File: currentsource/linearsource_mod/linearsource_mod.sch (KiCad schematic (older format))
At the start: 18 parts, among them P1 CONN_01X04, P2 CONN_01X04, Q1 PSMN017-30BL, Q2 BC849, U1 LM358

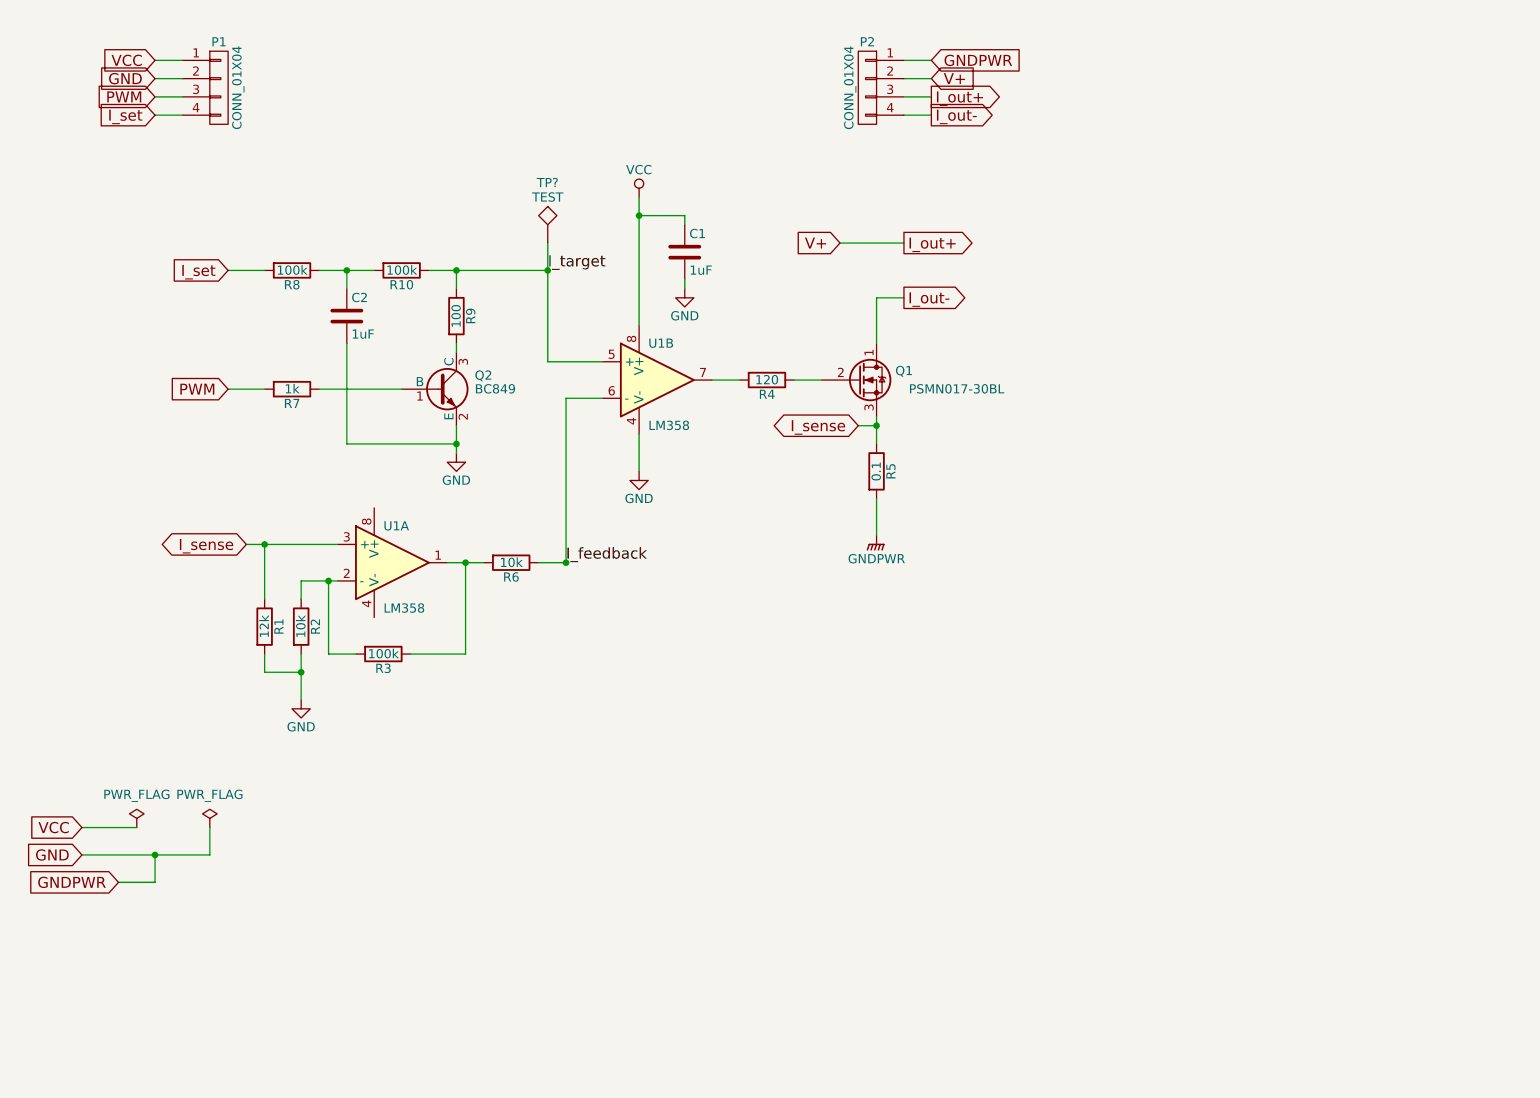
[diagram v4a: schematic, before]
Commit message: currentousrce: Change to edge header, incl Ifeedback
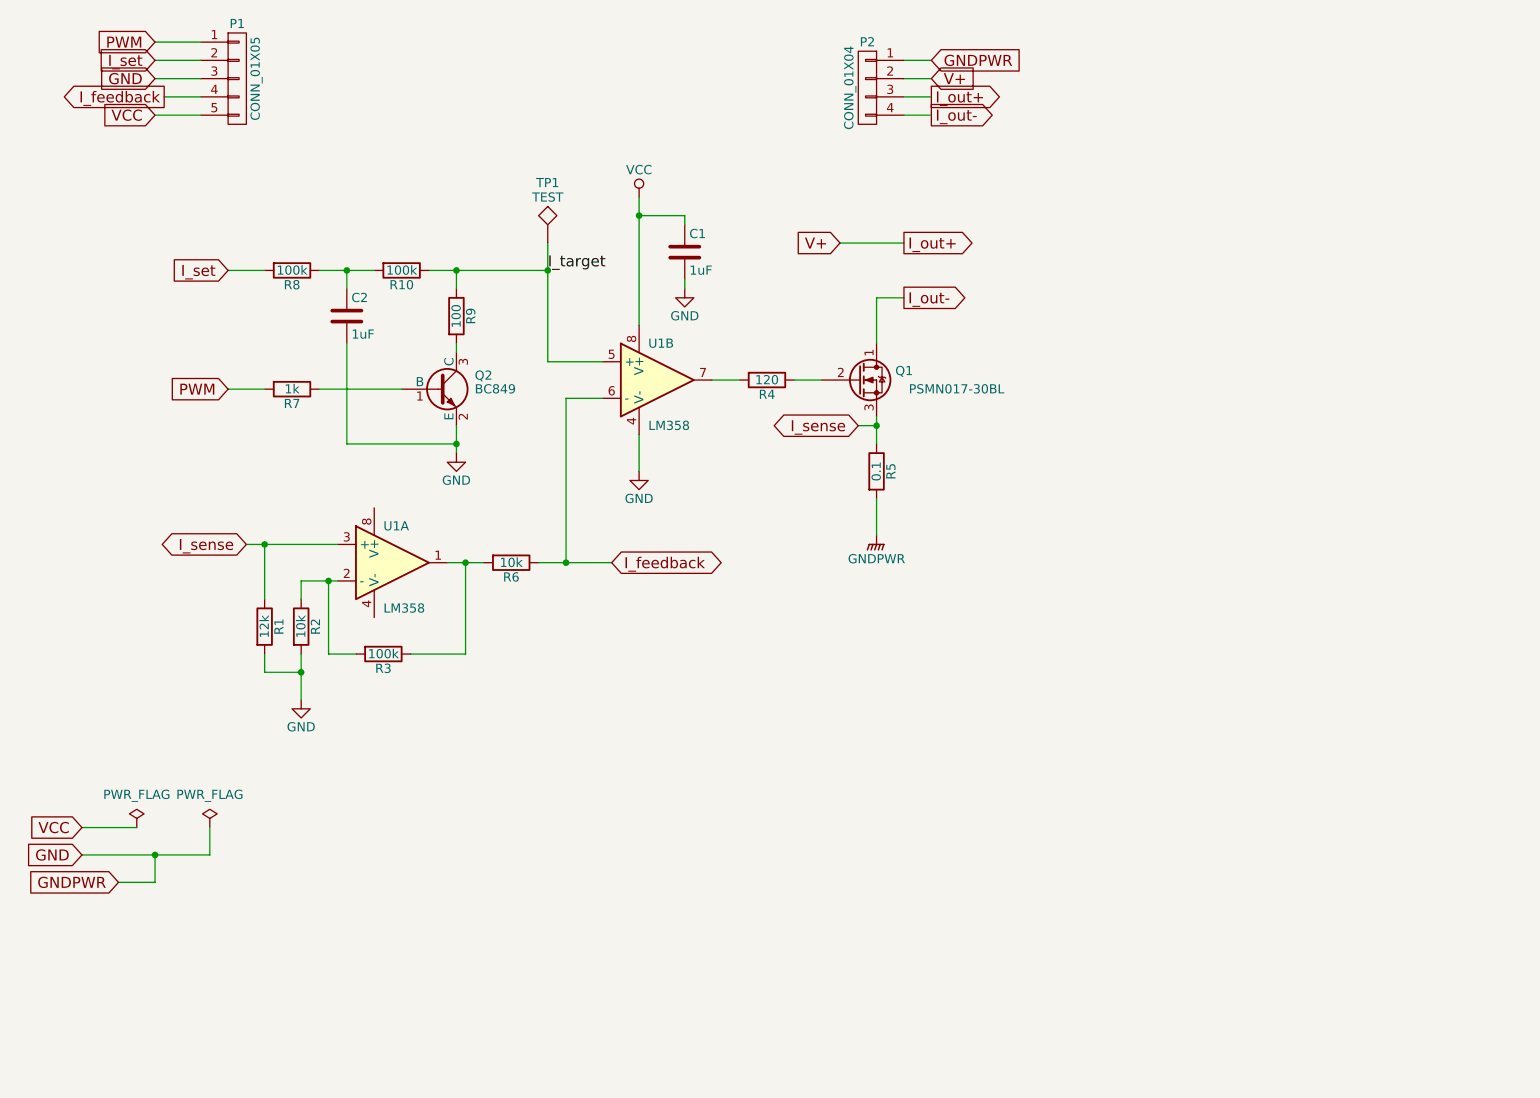
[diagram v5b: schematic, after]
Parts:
- removed P1: CONN_01X04, Pin_Headers:Pin_Header_Straight_1x04, symbol CONN_01X04
- added P1: CONN_01X05, Edge:Pin_Header_Edge_1x05_Pitch2.54mm, symbol CONN_01X05
- TP1: renamed from TP?; footprint (none) -> SMD_Packages:1Pin
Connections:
- net GND: now also P1.3 (P3)
- net I_feedback: now also P1.4 (P4)
- net I_set: now also P1.2 (P2)
- net PWM: now also P1.1 (P1)
- net VCC: now also P1.5 (P5)
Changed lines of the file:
@@
 	2900 4100 2900 3600
 Wire Wire Line
-	2000 3700 2150 3700
-Wire Wire Line
-	2150 3700 2200 3700
+	2000 3700 2200 3700
 Wire Wire Line
 	2000 3700 2000 3800
@@
 $EndComp
 Wire Wire Line
-	3850 1600 3850 1700
-Wire Wire Line
-	3850 1700 3850 2300
+	3850 1600 3850 2300
 Wire Wire Line
 	4700 2600 4850 2600
 Wire Wire Line
-	5150 2800 5150 2850
-Wire Wire Line
-	5150 2850 5150 2950
+	5150 2800 5150 2950
 Wire Wire Line
 	5150 3250 5150 3450
 Connection ~ 5150 2850
 Wire Wire Line
-	2000 4100 2000 4200
-Wire Wire Line
-	2000 4200 2000 4350
+	2000 4100 2000 4350
 Wire Wire Line
 	1800 3800 1800 3500
 Wire Wire Line
-	1700 3500 1800 3500
-Wire Wire Line
-	1800 3500 2200 3500
+	1700 3500 2200 3500
 Wire Wire Line
 	1800 4100 1800 4200
@@
 	4250 2600 4400 2600
 Wire Wire Line
-	2800 3600 2900 3600
-Wire Wire Line
-	2900 3600 3000 3600
+	2800 3600 3000 3600
 $Comp
 L R R6
@@
 	1    0    0    -1
 $EndComp
-$Comp
-L CONN_01X04 P1
-U 1 1 57115F44
-P 1550 1000
-F 0 "P1" H 1550 1250 50  0000 C CNN
-F 1 "CONN_01X04" V 1650 1000 50  0000 C CNN
-F 2 "Pin_Headers:Pin_Header_Straight_1x04" H 1550 1000 50  0001 C CNN
-F 3 "" H 1550 1000 50  0000 C CNN
-	1    1550 1000
-	1    0    0    -1
-$EndComp
-Text GLabel 1200 850  0    60   Input ~ 0
+Text GLabel 1200 1150 0    60   Input ~ 0
 VCC
-Text GLabel 1200 1050 0    60   Input ~ 0
+Text GLabel 1200 750  0    60   Input ~ 0
 PWM
 Text GLabel 1200 950  0    60   Input ~ 0
 GND
-Text GLabel 1200 1150 0    60   Input ~ 0
+Text GLabel 1200 850  0    60   Input ~ 0
 I_set
 $Comp
@@
 Wire Wire Line
 	5450 850  5300 850
-Wire Wire Line
-	1200 850  1350 850
-Wire Wire Line
-	1200 1150 1350 1150
 $Comp
 L C C1
@@
 $EndComp
 Wire Wire Line
-	2850 2850 2850 2950
-Wire Wire Line
-	2850 2950 2850 3000
+	2850 2850 2850 3000
 Wire Wire Line
 	2850 2450 2850 2400
@@
 	3350 2500 3650 2500
 Wire Wire Line
-	2100 2000 2250 2000
-Wire Wire Line
-	2250 2000 2400 2000
-Wire Wire Line
-	2700 2000 2850 2000
-Wire Wire Line
-	2850 2000 3350 2000
-Wire Wire Line
-	3350 1850 3350 2000
-Wire Wire Line
-	3350 2000 3350 2500
+	2100 2000 2400 2000
+Wire Wire Line
+	2700 2000 3350 2000
+Wire Wire Line
+	3350 1850 3350 2500
 Wire Wire Line
 	2850 2000 2850 2100
@@
 	1600 2650 1800 2650
 Wire Wire Line
-	3450 3600 3300 3600
+	3300 3600 3700 3600
 Text Label 3350 2000 0    60   ~ 0
 I_target
-Text Label 3450 3600 0    60   ~ 0
-I_feedback
 Connection ~ 3450 3600
 Connection ~ 3350 2000
@@
 	1500 5200 1500 5050
 Wire Wire Line
-	800  5200 1200 5200
-Wire Wire Line
-	1200 5200 1500 5200
+	800  5200 1500 5200
 Wire Wire Line
 	1000 5350 1200 5350
@@
 	0    1    1    0
 $EndComp
-Wire Wire Line
-	1200 1050 1350 1050
-Wire Wire Line
-	1200 950  1350 950
-$Comp
-L TEST TP?
+$Comp
+L TEST TP1
 U 1 1 598733DB
 P 3350 1850
-F 0 "TP?" H 3350 2150 50  0000 C BNN
+F 0 "TP1" H 3350 2150 50  0000 C BNN
 F 1 "TEST" H 3350 2100 50  0000 C CNN
-F 2 "" H 3350 1850 50  0001 C CNN
+F 2 "SMD_Packages:1Pin" H 3350 1850 50  0001 C CNN
 F 3 "" H 3350 1850 50  0001 C CNN
 	1    3350 1850
 	1    0    0    -1
 $EndComp
+Text GLabel 3700 3600 2    60   BiDi ~ 0
+I_feedback
+$Comp
+L CONN_01X05 P1
+U 1 1 59873CDC
+P 1650 950
+F 0 "P1" H 1650 1250 50  0000 C CNN
+F 1 "CONN_01X05" V 1750 950 50  0000 C CNN
+F 2 "Edge:Pin_Header_Edge_1x05_Pitch2.54mm" H 1650 950 50  0001 C CNN
+F 3 "" H 1650 950 50  0001 C CNN
+	1    1650 950
+	1    0    0    -1
+$EndComp
+Text GLabel 1250 1050 0    60   Output ~ 0
+I_feedback
+Wire Wire Line
+	1200 950  1450 950
+Wire Wire Line
+	1250 1050 1450 1050
+Wire Wire Line
+	1200 1150 1450 1150
+Wire Wire Line
+	1200 850  1450 850
+Wire Wire Line
+	1200 750  1450 750
 $EndSCHEMATC

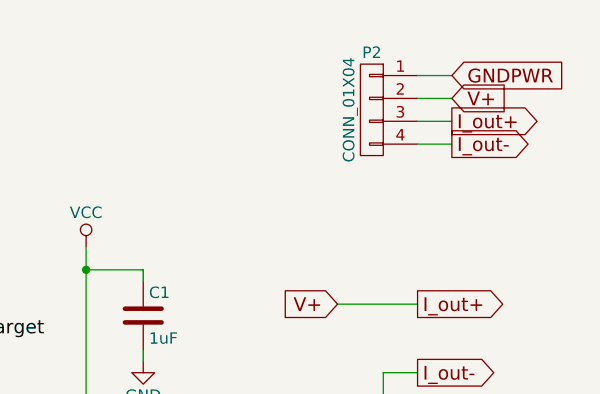
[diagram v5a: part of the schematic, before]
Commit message: currentsource: Use edge header also for power
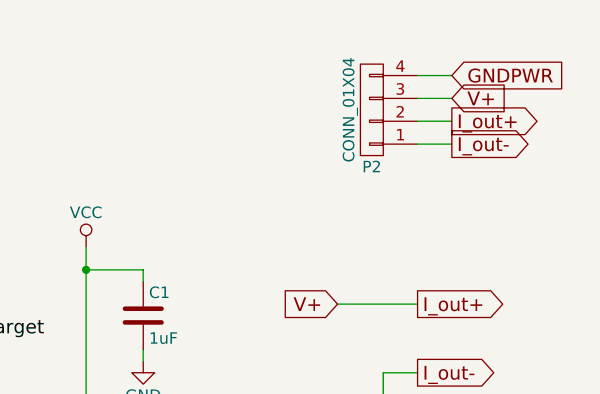
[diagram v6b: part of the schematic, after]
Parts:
- P2: footprint Pin_Headers:Pin_Header_Straight_1x04 -> (none)
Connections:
- net GND: now also P2.4 (P4); no longer P2.1 (P1)
- net I_out-: now also P2.1 (P1); no longer P2.4 (P4)
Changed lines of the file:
@@
 	1    0    0    -1
 $EndComp
-Wire Wire Line
-	2600 4100 2900 4100
-Wire Wire Line
-	2900 4100 2900 3600
-Wire Wire Line
-	2000 3700 2200 3700
-Wire Wire Line
-	2000 3700 2000 3800
-Wire Wire Line
-	2300 4100 2150 4100
-Wire Wire Line
-	2150 4100 2150 3700
-Connection ~ 2150 3700
-Wire Wire Line
-	3850 2900 3850 3100
 $Comp
 L VCC #PWR01
@@
 	1    0    0    -1
 $EndComp
-Wire Wire Line
-	3850 1600 3850 2300
-Wire Wire Line
-	4700 2600 4850 2600
-Wire Wire Line
-	5150 2800 5150 2950
-Wire Wire Line
-	5150 3250 5150 3450
-Connection ~ 5150 2850
-Wire Wire Line
-	2000 4100 2000 4350
-Wire Wire Line
-	1800 3800 1800 3500
-Wire Wire Line
-	1700 3500 2200 3500
-Wire Wire Line
-	1800 4100 1800 4200
-Wire Wire Line
-	1800 4200 2000 4200
-Connection ~ 2000 4200
 Text GLabel 5050 2850 0    60   BiDi ~ 0
 I_sense
-Wire Wire Line
-	5050 2850 5150 2850
 Text GLabel 1700 3500 0    60   BiDi ~ 0
 I_sense
-Connection ~ 1800 3500
-Connection ~ 2900 3600
-Wire Wire Line
-	5150 2150 5150 2400
-Wire Wire Line
-	4250 2600 4400 2600
-Wire Wire Line
-	2800 3600 3000 3600
 $Comp
 L R R6
@@
 	0    1    1    0
 $EndComp
-Wire Wire Line
-	3450 2700 3450 3600
-Wire Wire Line
-	3450 2700 3650 2700
 $Comp
 L GNDPWR #PWR02
@@
 Text GLabel 1200 850  0    60   Input ~ 0
 I_set
-$Comp
-L CONN_01X04 P2
-U 1 1 571160BF
-P 5100 1000
-F 0 "P2" H 5100 1250 50  0000 C CNN
-F 1 "CONN_01X04" V 5200 1000 50  0000 C CNN
-F 2 "Pin_Headers:Pin_Header_Straight_1x04" H 5100 1000 50  0001 C CNN
-F 3 "" H 5100 1000 50  0000 C CNN
-	1    5100 1000
-	-1   0    0    -1
-$EndComp
 Text GLabel 5450 850  2    60   Input ~ 0
 GNDPWR
@@
 Text GLabel 4950 1850 0    60   Input ~ 0
 V+
-Wire Wire Line
-	5450 1150 5300 1150
-Wire Wire Line
-	5450 1050 5300 1050
-Wire Wire Line
-	5450 950  5300 950
-Wire Wire Line
-	5450 850  5300 850
 $Comp
 L C C1
@@
 	1    0    0    -1
 $EndComp
-Wire Wire Line
-	4100 1700 4100 1750
-Wire Wire Line
-	4100 2050 4100 2100
 $Comp
 L GND #PWR03
@@
 	0    1    1    0
 $EndComp
-Wire Wire Line
-	2850 2850 2850 3000
-Wire Wire Line
-	2850 2450 2850 2400
-Wire Wire Line
-	2100 2650 2550 2650
-Wire Wire Line
-	3350 2500 3650 2500
-Wire Wire Line
-	2100 2000 2400 2000
-Wire Wire Line
-	2700 2000 3350 2000
-Wire Wire Line
-	3350 1850 3350 2500
-Wire Wire Line
-	2850 2000 2850 2100
 $Comp
 L C C2
@@
 	0    1    1    0
 $EndComp
-Wire Wire Line
-	2250 2000 2250 2100
-Connection ~ 2250 2000
-Connection ~ 2850 2000
 Text GLabel 1600 2000 0    60   Input ~ 0
 I_set
-Wire Wire Line
-	1600 2000 1800 2000
-Wire Wire Line
-	2250 2400 2250 2950
-Wire Wire Line
-	2250 2950 2850 2950
-Connection ~ 2850 2950
 Text GLabel 1600 2650 0    60   Input ~ 0
 PWM
-Wire Wire Line
-	1600 2650 1800 2650
-Wire Wire Line
-	3300 3600 3700 3600
 Text Label 3350 2000 0    60   ~ 0
 I_target
-Connection ~ 3450 3600
-Connection ~ 3350 2000
-Wire Wire Line
-	5300 2150 5150 2150
-Wire Wire Line
-	4950 1850 5300 1850
-Wire Wire Line
-	4100 1700 3850 1700
-Connection ~ 3850 1700
 Text GLabel 800  5050 0    60   Input ~ 0
 VCC
@@
 	1    0    0    -1
 $EndComp
-Wire Wire Line
-	1100 5050 800  5050
-Wire Wire Line
-	1500 5200 1500 5050
-Wire Wire Line
-	800  5200 1500 5200
-Wire Wire Line
-	1000 5350 1200 5350
-Wire Wire Line
-	1200 5350 1200 5200
-Connection ~ 1200 5200
 $Comp
 L R R10
@@
 I_feedback
 Wire Wire Line
+	2600 4100 2900 4100
+Wire Wire Line
+	2900 4100 2900 3600
+Wire Wire Line
+	2000 3700 2200 3700
+Wire Wire Line
+	2000 3700 2000 3800
+Wire Wire Line
+	2300 4100 2150 4100
+Wire Wire Line
+	2150 4100 2150 3700
+Connection ~ 2150 3700
+Wire Wire Line
+	3850 2900 3850 3100
+Wire Wire Line
+	3850 1600 3850 2300
+Wire Wire Line
+	4700 2600 4850 2600
+Wire Wire Line
+	5150 2800 5150 2950
+Wire Wire Line
+	5150 3250 5150 3450
+Connection ~ 5150 2850
+Wire Wire Line
+	2000 4100 2000 4350
+Wire Wire Line
+	1800 3800 1800 3500
+Wire Wire Line
+	1700 3500 2200 3500
+Wire Wire Line
+	1800 4100 1800 4200
+Wire Wire Line
+	1800 4200 2000 4200
+Connection ~ 2000 4200
+Wire Wire Line
+	5050 2850 5150 2850
+Connection ~ 1800 3500
+Connection ~ 2900 3600
+Wire Wire Line
+	5150 2150 5150 2400
+Wire Wire Line
+	4250 2600 4400 2600
+Wire Wire Line
+	2800 3600 3000 3600
+Wire Wire Line
+	3450 2700 3450 3600
+Wire Wire Line
+	3450 2700 3650 2700
+Wire Wire Line
+	4100 1700 4100 1750
+Wire Wire Line
+	4100 2050 4100 2100
+Wire Wire Line
+	2850 2850 2850 3000
+Wire Wire Line
+	2850 2450 2850 2400
+Wire Wire Line
+	2100 2650 2550 2650
+Wire Wire Line
+	3350 2500 3650 2500
+Wire Wire Line
+	2100 2000 2400 2000
+Wire Wire Line
+	2700 2000 3350 2000
+Wire Wire Line
+	3350 1850 3350 2500
+Wire Wire Line
+	2850 2000 2850 2100
+Wire Wire Line
+	2250 2000 2250 2100
+Connection ~ 2250 2000
+Connection ~ 2850 2000
+Wire Wire Line
+	1600 2000 1800 2000
+Wire Wire Line
+	2250 2400 2250 2950
+Wire Wire Line
+	2250 2950 2850 2950
+Connection ~ 2850 2950
+Wire Wire Line
+	1600 2650 1800 2650
+Wire Wire Line
+	3300 3600 3700 3600
+Connection ~ 3450 3600
+Connection ~ 3350 2000
+Wire Wire Line
+	5300 2150 5150 2150
+Wire Wire Line
+	4950 1850 5300 1850
+Wire Wire Line
+	4100 1700 3850 1700
+Connection ~ 3850 1700
+Wire Wire Line
+	1100 5050 800  5050
+Wire Wire Line
+	1500 5200 1500 5050
+Wire Wire Line
+	800  5200 1500 5200
+Wire Wire Line
+	1000 5350 1200 5350
+Wire Wire Line
+	1200 5350 1200 5200
+Connection ~ 1200 5200
+Wire Wire Line
 	1200 950  1450 950
 Wire Wire Line
@@
 Wire Wire Line
 	1200 750  1450 750
+$Comp
+L CONN_01X04 P2
+U 1 1 59875E7B
+P 5100 1000
+F 0 "P2" H 5100 1250 50  0000 C CNN
+F 1 "CONN_01X04" V 5200 1000 50  0000 C CNN
+F 2 "" H 5100 1000 50  0001 C CNN
+F 3 "" H 5100 1000 50  0001 C CNN
+	1    5100 1000
+	-1   0    0    1
+$EndComp
+Wire Wire Line
+	5300 1150 5450 1150
+Wire Wire Line
+	5300 1050 5450 1050
+Wire Wire Line
+	5300 950  5450 950
+Wire Wire Line
+	5300 850  5450 850
 $EndSCHEMATC
